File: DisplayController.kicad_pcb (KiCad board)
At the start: 2 copper layers, 42.5 x 71.8 mm, 31 parts, among them IC1 LM2937IMP-5.0, IC2 LM2937IMP-3.3, P1 PWR, P2 OUTPUT, P3 Programming Header, Q1 PZT2222A, Q2 PZT2222A, Q3 PZT2222A, Q4 PZT2222A, U1 ESP-12E

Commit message: Adding a logo and GND plane on both sides
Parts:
- added G***: LOGO, DisplayController:Brett-Logo-small, B.Cu at (166.4, 120.0)
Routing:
- net +5V: track 32.7 -> 87.7 mm
- net GND: track 31.5 -> 19.0 mm, vias 4 -> 1
- net (no net): vias 0 -> 1
- added copper zone on B.Cu, net GND
- removed copper zone on B.Cu, net +3V3
- removed copper zone on B.Cu, net +5V
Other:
- board text added: ""A Momentary Lapse of Sanity 2.0""
- board text added: "@bjmaz"
- board text added: "A Brett Wilkins Creation"
- board text removed: "A Momentary Lapse of Sanity 2.0"

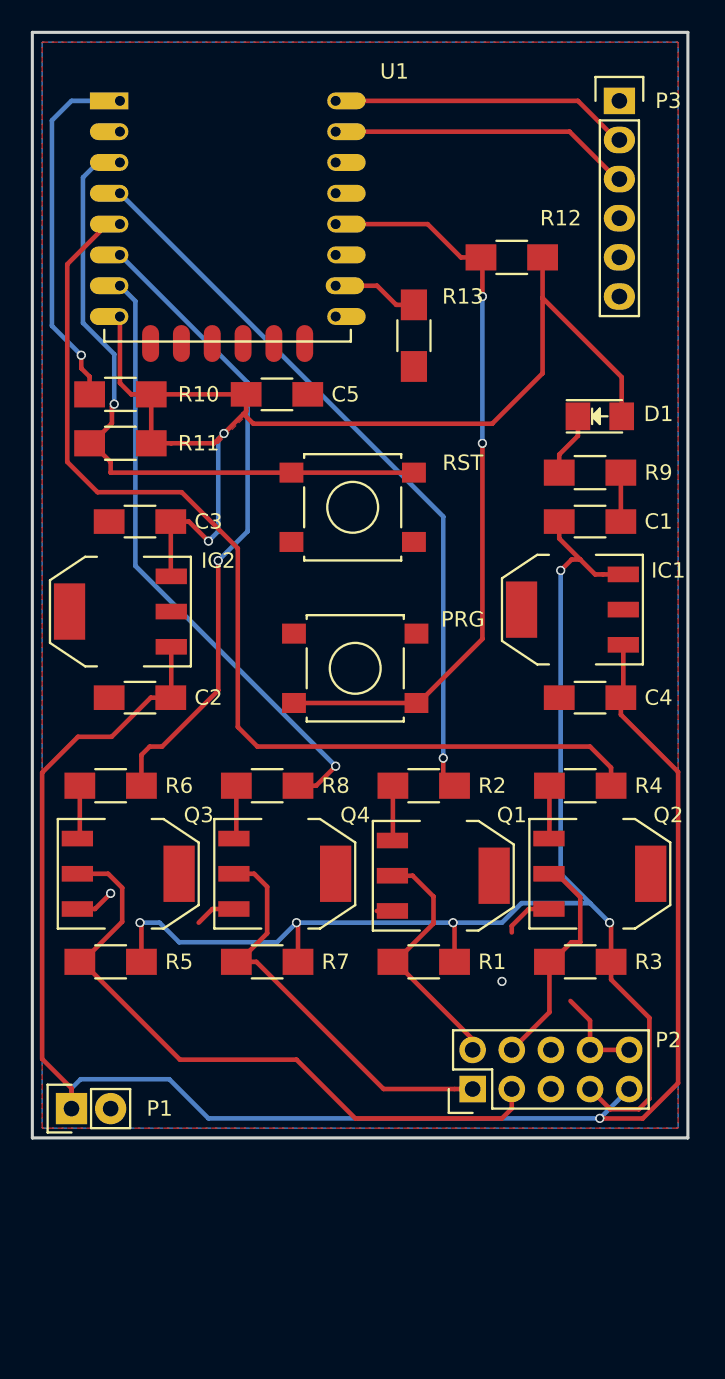
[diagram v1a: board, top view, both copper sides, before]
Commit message: WIP: converted ESP footprint to SMD (pads). Now rerouting and changing configuration of signal pins so that signal routing is easier.
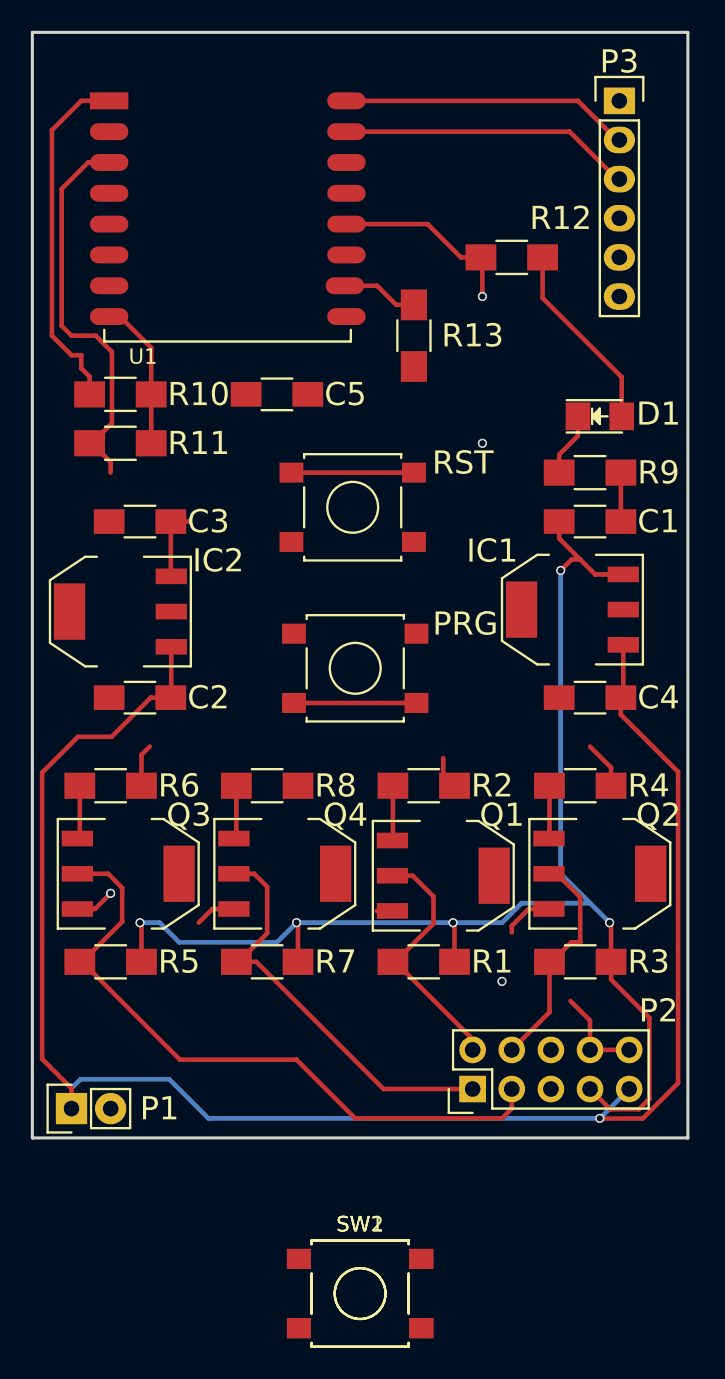
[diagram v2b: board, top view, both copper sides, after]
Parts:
- added SW1: RST, Buttons_Switches_SMD:SW_SPST_B3S-1000, F.Cu at (158.4, 145.4)
- added SW2: PRG, Buttons_Switches_SMD:SW_SPST_B3S-1000, F.Cu at (158.4, 145.4)
- U1: value ESP-12E -> ESP-12; footprint ESP8266:ESP-12E -> ESP8266:ESP-12-SMD
- moved G*** 0.90 mm to (165.7, 119.4)
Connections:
- U1 pad 10: Net-(U1-Pad10) -> Net-(R13-Pad2)
- U1 pad 12: Net-(U1-Pad12) -> Net-(R12-Pad2)
- U1 pad 15: GND -> Net-(P3-Pad3)
- U1 pad 16: Net-(R13-Pad2) -> Net-(P3-Pad2)
- U1 pad 9: Net-(U1-Pad9) -> GND
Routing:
- net Net-(R4-Pad2): track 68.8 -> 3.92 mm
- net +3V3: track 76.4 -> 26.3 mm, vias 2 -> 0
- net Net-(R2-Pad2): track 47.4 -> 2.09 mm, vias 1 -> 0
- net Net-(R8-Pad2): track 40.0 -> 0.00 mm, vias 1 -> 0
- net Net-(R6-Pad2): track 41.2 -> 2.76 mm, vias 1 -> 0
- net Net-(R12-Pad2): track 49.1 -> 21.0 mm
- net Net-(R11-Pad1): track 43.7 -> 34.3 mm, vias 1 -> 0
- net Net-(R10-Pad1): vias 1 -> 0
- removed copper zone on F.Cu, net +3V3
- removed copper zone on B.Cu, net GND
- removed copper zone on F.Cu, net GND

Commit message: rev2, About to create Gerbers
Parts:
- removed PRG: PRG, Buttons_Switches_SMD:SW_SPST_B3S-1000
- removed RST: RST, Buttons_Switches_SMD:SW_SPST_B3S-1000
- moved SW1 50.7 mm to (158.1, 94.6)
- moved SW2 40.6 mm to (158.1, 104.8)
- moved U1 1.78 mm to (142.8, 66.2)
- moved G*** 1.42 mm to (166.4, 120.7)
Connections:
- U1 pad 4: Net-(R2-Pad2) -> Net-(R4-Pad2)
- U1 pad 5: Net-(R4-Pad2) -> Net-(R2-Pad2)
- U1 pad 6: Net-(R6-Pad2) -> Net-(R8-Pad2)
- U1 pad 7: Net-(R8-Pad2) -> Net-(R6-Pad2)
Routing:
- net Net-(R4-Pad2): track 3.92 -> 55.0 mm
- net Net-(R2-Pad2): track 2.09 -> 50.2 mm
- net Net-(R8-Pad2): track 0.00 -> 41.0 mm
- net Net-(R6-Pad2): track 2.76 -> 41.4 mm
- net +3V3: track 26.3 -> 64.3 mm, vias 0 -> 3
- net Net-(R12-Pad2): track 21.0 -> 50.7 mm
- net Net-(R11-Pad1): track 34.3 -> 51.6 mm, vias 0 -> 2
- net Net-(R10-Pad1): track 23.7 -> 25.7 mm
- net Net-(R13-Pad2): track 5.59 -> 6.33 mm
- net Net-(P3-Pad2): track 19.5 -> 20.2 mm
- net Net-(P3-Pad3): track 19.7 -> 20.4 mm
- net GND: track 19.0 -> 19.4 mm, vias 1 -> 5
- added copper zone on B.Cu, net GND
- added copper zone on F.Cu, net GND

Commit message: Board should be ready to go
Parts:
- moved G*** 6.86 mm to (166.4, 113.8)
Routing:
- net +3V3: track 64.3 -> 63.1 mm
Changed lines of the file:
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@@
 (kicad_pcb (version 4) (host pcbnew 4.0.4-stable)
   (general
-    (links 0)
+    (links 68)
     (no_connects 0)
     (area 135.525 57.091999 196.445 144.940001)
     (thickness 1.6)
     (drawings 9)
-    (tracks 241)
+    (tracks 240)
     (zones 0)
     (modules 32)
@@
   )
   (page A4)
+  (title_block
+    (title "A Momentary Lapse of Sanity")
+    (date 2016-12-10)
+    (rev 2)
+    (company "A Brett Wilkins Creation")
+  )
   (layers
     (0 F.Cu signal)
@@
     (tags "capacitor 1206")
     (attr smd)
-    (fp_text reference C1 (at 4.445 0) (layer F.SilkS)
+    (fp_text reference C1 (at 4.445 -1.778) (layer F.SilkS)
       (effects (font (size 1.5 1.5) (thickness 0.25)))
     )
@@
     (tags "capacitor 1206")
     (attr smd)
-    (fp_text reference C2 (at -4.445 0 180) (layer F.SilkS)
+    (fp_text reference C2 (at -5.08 0 180) (layer F.SilkS)
       (effects (font (size 1.5 1.5) (thickness 0.25)))
     )
@@
     (tags "capacitor 1206")
     (attr smd)
-    (fp_text reference C3 (at -4.445 0 180) (layer F.SilkS)
+    (fp_text reference C3 (at -5.08 0 180) (layer F.SilkS)
       (effects (font (size 1.5 1.5) (thickness 0.25)))
     )
@@
     (tags "capacitor 1206")
     (attr smd)
-    (fp_text reference C4 (at -4.445 0 180) (layer F.SilkS)
+    (fp_text reference C4 (at -4.445 1.524 180) (layer F.SilkS)
       (effects (font (size 1.5 1.5) (thickness 0.25)))
     )
@@
     (tags "LED1206 SMD")
     (attr smd)
-    (fp_text reference D1 (at 3.81 -0.155362) (layer F.SilkS)
+    (fp_text reference D1 (at 3.81 -2.568362) (layer F.SilkS)
       (effects (font (size 1.5 1.5) (thickness 0.25)))
     )
@@
     (tags "CMS SOT")
     (attr smd)
-    (fp_text reference IC2 (at 3.302 6.35 180) (layer F.SilkS)
+    (fp_text reference IC2 (at 3.302 6.985 180) (layer F.SilkS)
       (effects (font (size 1.5 1.5) (thickness 0.25)))
     )
@@
     (tags "resistor 1206")
     (attr smd)
-    (fp_text reference R1 (at 4.445 0) (layer F.SilkS)
+    (fp_text reference R1 (at 5.08 0) (layer F.SilkS)
       (effects (font (size 1.5 1.5) (thickness 0.25)))
     )
@@
     (tags "resistor 1206")
     (attr smd)
-    (fp_text reference R2 (at 4.445 0) (layer F.SilkS)
+    (fp_text reference R2 (at 5.08 -1.905) (layer F.SilkS)
       (effects (font (size 1.5 1.5) (thickness 0.25)))
     )
@@
     (tags "resistor 1206")
     (attr smd)
-    (fp_text reference R3 (at 4.445 0) (layer F.SilkS)
+    (fp_text reference R3 (at 5.08 0) (layer F.SilkS)
       (effects (font (size 1.5 1.5) (thickness 0.25)))
     )
@@
     (tags "resistor 1206")
     (attr smd)
-    (fp_text reference R4 (at 4.445 0) (layer F.SilkS)
+    (fp_text reference R4 (at 5.08 -1.905) (layer F.SilkS)
       (effects (font (size 1.5 1.5) (thickness 0.25)))
     )
@@
     (tags "resistor 1206")
     (attr smd)
-    (fp_text reference R5 (at 4.445 0) (layer F.SilkS)
+    (fp_text reference R5 (at 5.08 0) (layer F.SilkS)
       (effects (font (size 1.5 1.5) (thickness 0.25)))
     )
@@
     (tags "resistor 1206")
     (attr smd)
-    (fp_text reference R6 (at 4.445 0) (layer F.SilkS)
+    (fp_text reference R6 (at 5.08 -1.905) (layer F.SilkS)
       (effects (font (size 1.5 1.5) (thickness 0.25)))
     )
@@
     (tags "resistor 1206")
     (attr smd)
-    (fp_text reference R7 (at 4.445 0) (layer F.SilkS)
+    (fp_text reference R7 (at 5.08 0) (layer F.SilkS)
       (effects (font (size 1.5 1.5) (thickness 0.25)))
     )
@@
     (tags "resistor 1206")
     (attr smd)
-    (fp_text reference R8 (at 4.445 0) (layer F.SilkS)
+    (fp_text reference R8 (at 5.08 -1.905) (layer F.SilkS)
       (effects (font (size 1.5 1.5) (thickness 0.25)))
     )
@@
     (tags "resistor 1206")
     (attr smd)
-    (fp_text reference R9 (at -4.445 0 180) (layer F.SilkS)
+    (fp_text reference R9 (at -4.445 1.651 180) (layer F.SilkS)
       (effects (font (size 1.5 1.5) (thickness 0.25)))
     )
@@
     (tags "resistor 1206")
     (attr smd)
-    (fp_text reference R10 (at 5.08 0) (layer F.SilkS)
+    (fp_text reference R10 (at -0.127 -2.159) (layer F.SilkS)
       (effects (font (size 1.5 1.5) (thickness 0.25)))
     )
@@
     (tags "resistor 1206")
     (attr smd)
-    (fp_text reference R11 (at 5.08 0) (layer F.SilkS)
+    (fp_text reference R11 (at 5.715 0) (layer F.SilkS)
       (effects (font (size 1.5 1.5) (thickness 0.25)))
     )
@@
     (descr "Module, ESP-8266, ESP-12, 16 pad, SMD")
     (tags "Module ESP-8266 ESP8266")
-    (fp_text reference U1 (at 1.5 16.6) (layer F.SilkS)
-      (effects (font (size 1 1) (thickness 0.15)))
+    (fp_text reference U1 (at 17.683 -1.143) (layer F.SilkS)
+      (effects (font (size 1.5 1.5) (thickness 0.25)))
     )
     (fp_text value ESP-12 (at 6.992 1) (layer F.Fab)
@@
   )
   (module DisplayController:Brett-Logo-small (layer B.Cu)
-    (at 166.37 120.65 270)
+    (at 166.37 113.792 270)
     (fp_text reference G*** (at 0 0 270) (layer B.SilkS) hide
       (effects (font (thickness 0.3)) (justify mirror))
@@
   (segment (start 144.845 94.15) (end 145.945 95.25) (width 0.3) (layer F.Cu) (net 4))
   (segment (start 145.945 95.25) (end 146.145 95.25) (width 0.3) (layer F.Cu) (net 4))
-  (segment (start 146.145 95.25) (end 147.32 95.25) (width 0.3) (layer F.Cu) (net 4))
   (segment (start 146.145 95.25) (end 146.145 98.774) (width 0.3) (layer F.Cu) (net 4))
   (segment (start 146.145 98.774) (end 146.177 98.806) (width 0.3) (layer F.Cu) (net 4))

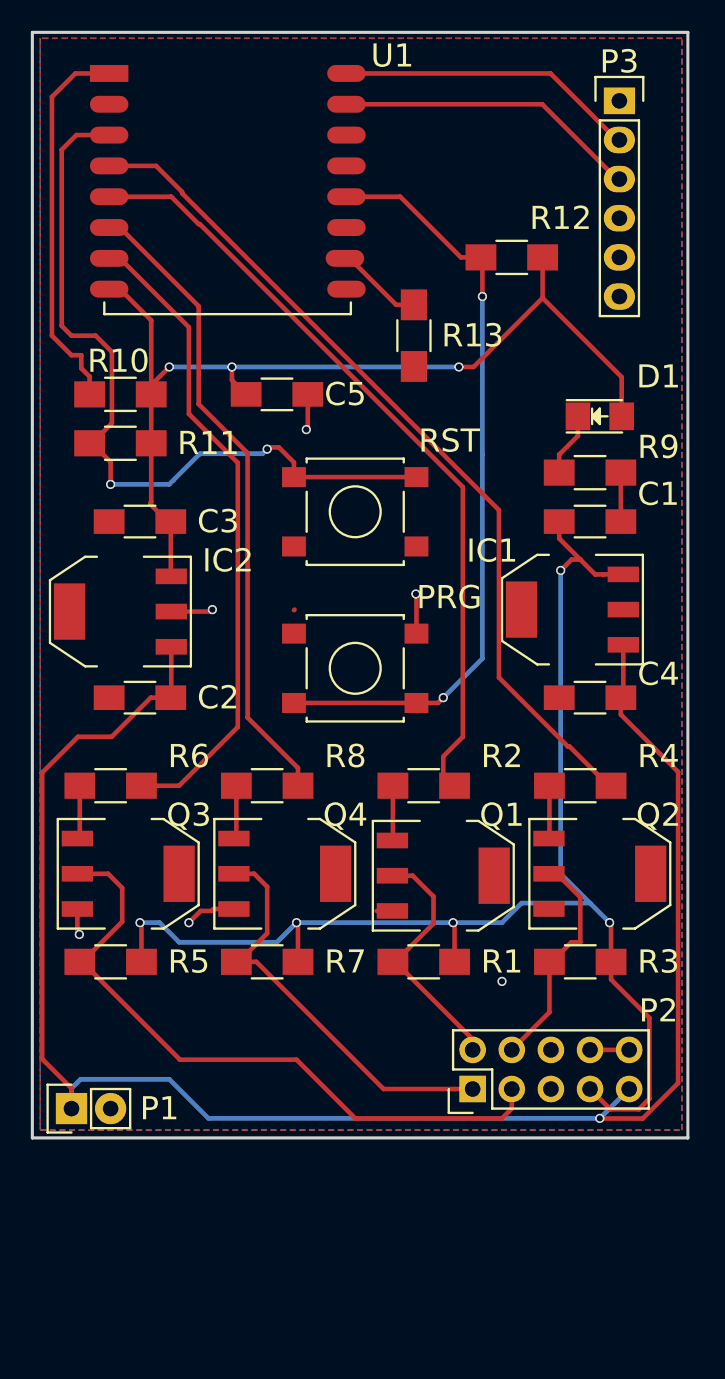
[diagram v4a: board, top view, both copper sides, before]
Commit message: Changing SOT-223 footprint to SOT-23-3. Respin and resize of the board.
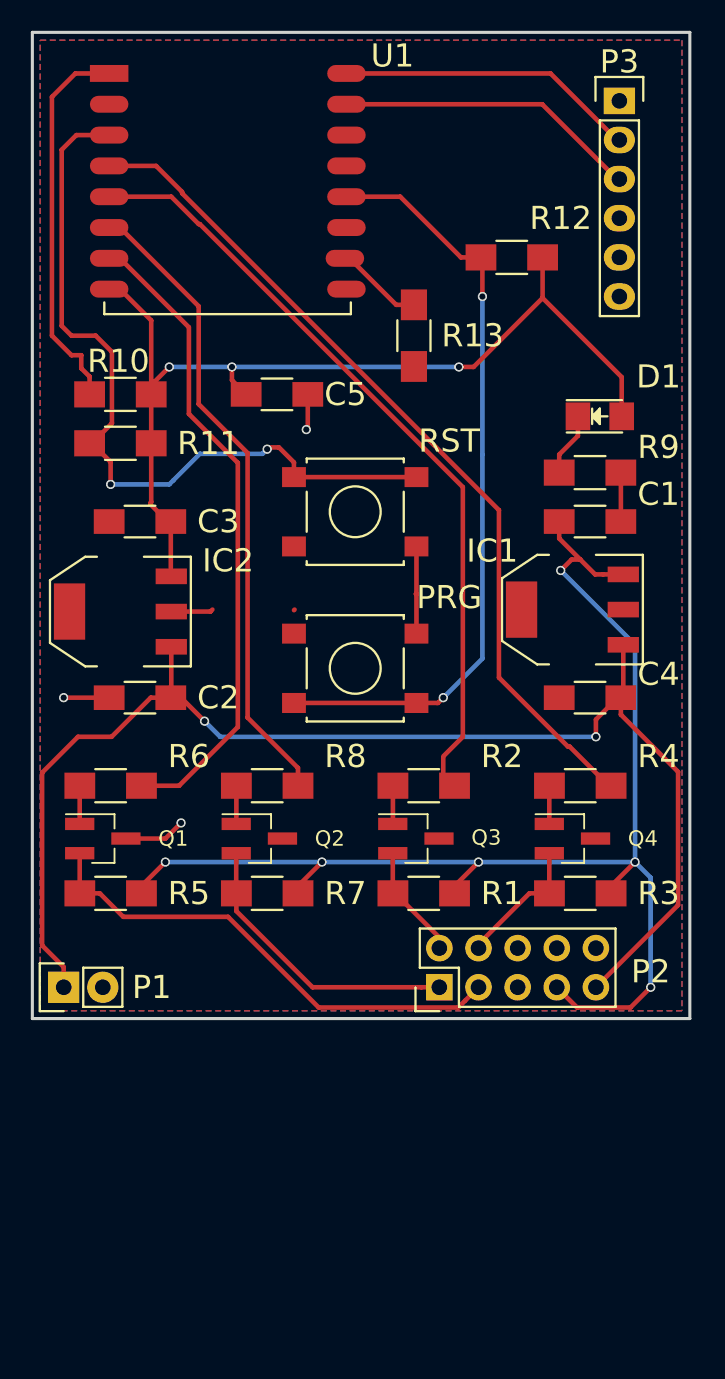
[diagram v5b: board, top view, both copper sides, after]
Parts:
- Q1, Q2, Q3, Q4: value PZT2222A -> SMBT2222A; footprint TO_SOT_Packages_SMD:SOT-223 -> TO_SOT_Packages_SMD:SOT-23_Handsoldering
- moved Q1 22.2 mm to (141.7, 115.8), turned to 0 degrees
- moved Q2 22.2 mm to (151.9, 115.8), turned to 0 degrees
- moved Q3 18.8 mm to (162.1, 115.8), turned to 0 degrees
- moved Q4 18.8 mm to (172.2, 115.8), turned to 0 degrees
- moved P1 7.89 mm to (139.2, 125.5)
- moved P2 6.95 mm to (163.6, 125.5)
- moved R1 4.45 mm to (162.6, 119.4)
- moved R3 4.45 mm to (172.7, 119.4)
- moved R5 4.45 mm to (142.2, 119.4)
- moved R7 4.45 mm to (152.4, 119.4)
- moved G*** 3.57 mm to (166.1, 110.2)
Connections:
- Q1 pad 2: Net-(P2-Pad2) -> Net-(P2-Pad3)
- Q2 pad 2: Net-(P2-Pad4) -> Net-(P2-Pad1)
- Q3 pad 2: Net-(P2-Pad3) -> Net-(P2-Pad2)
- Q4 pad 2: Net-(P2-Pad1) -> Net-(P2-Pad4)
- R2 pad 1: Net-(Q1-Pad1) -> Net-(Q3-Pad1)
- R4 pad 1: Net-(Q2-Pad1) -> Net-(Q4-Pad1)
- R6 pad 1: Net-(Q3-Pad1) -> Net-(Q1-Pad1)
- R8 pad 1: Net-(Q4-Pad1) -> Net-(Q2-Pad1)
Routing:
- net +9V: track 112.5 -> 86.7 mm, vias 1 -> 2
- net Net-(P2-Pad3): track 42.9 -> 32.1 mm
- net Net-(P2-Pad2): track 16.4 -> 7.50 mm
- net Net-(P2-Pad1): track 27.2 -> 19.0 mm
- net Net-(P2-Pad4): track 14.8 -> 8.83 mm
- net +5V: track 87.7 -> 85.6 mm, vias 5 -> 6
- net GND: track 19.4 -> 20.9 mm, vias 5 -> 3
- net Net-(Q1-Pad1): track 3.57 -> 2.48 mm
- net Net-(Q3-Pad1): track 3.49 -> 2.49 mm
- net Net-(Q2-Pad1): track 3.49 -> 2.49 mm
- net Net-(Q4-Pad1): track 3.49 -> 2.53 mm
- net (no net): vias 1 -> 0
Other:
- board size 42.5 x 71.8 mm -> 42.7 x 64 mm
